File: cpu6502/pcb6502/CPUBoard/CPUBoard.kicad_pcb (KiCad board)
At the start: 2 copper layers, 108.5 x 60.8 mm, 26 parts, among them J1 Expansion, J3 DC Power, J4 Ext Pwr Sw, SW1 Reset, U2 6502 (CPU), U3 28C256 (ROM), U4 L7805, U5 62256 (RAM), U6 DS1813, X1 1MHz

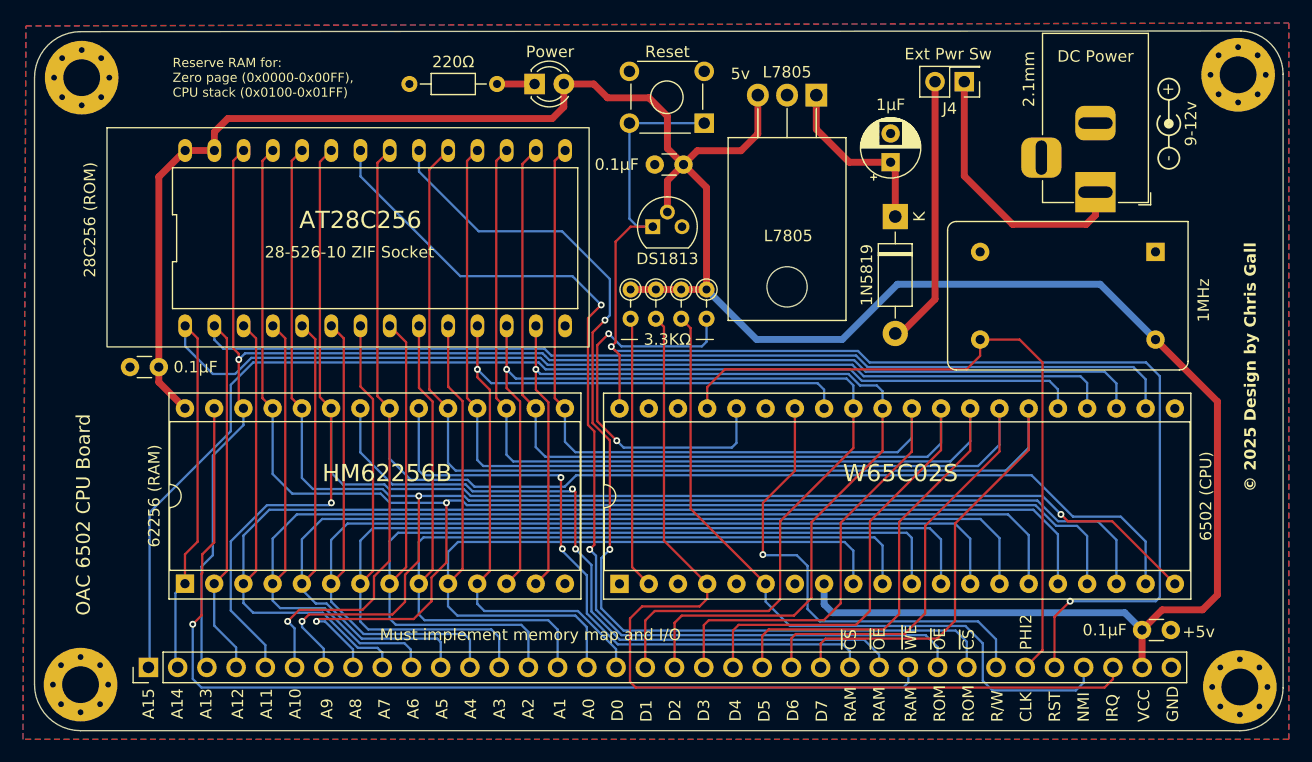
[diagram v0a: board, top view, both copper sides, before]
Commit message: dialed in zeropage and inputbuffer length
PCB CPU BOARD SENT WOOOO HOOO!!
tweaked basic tokens
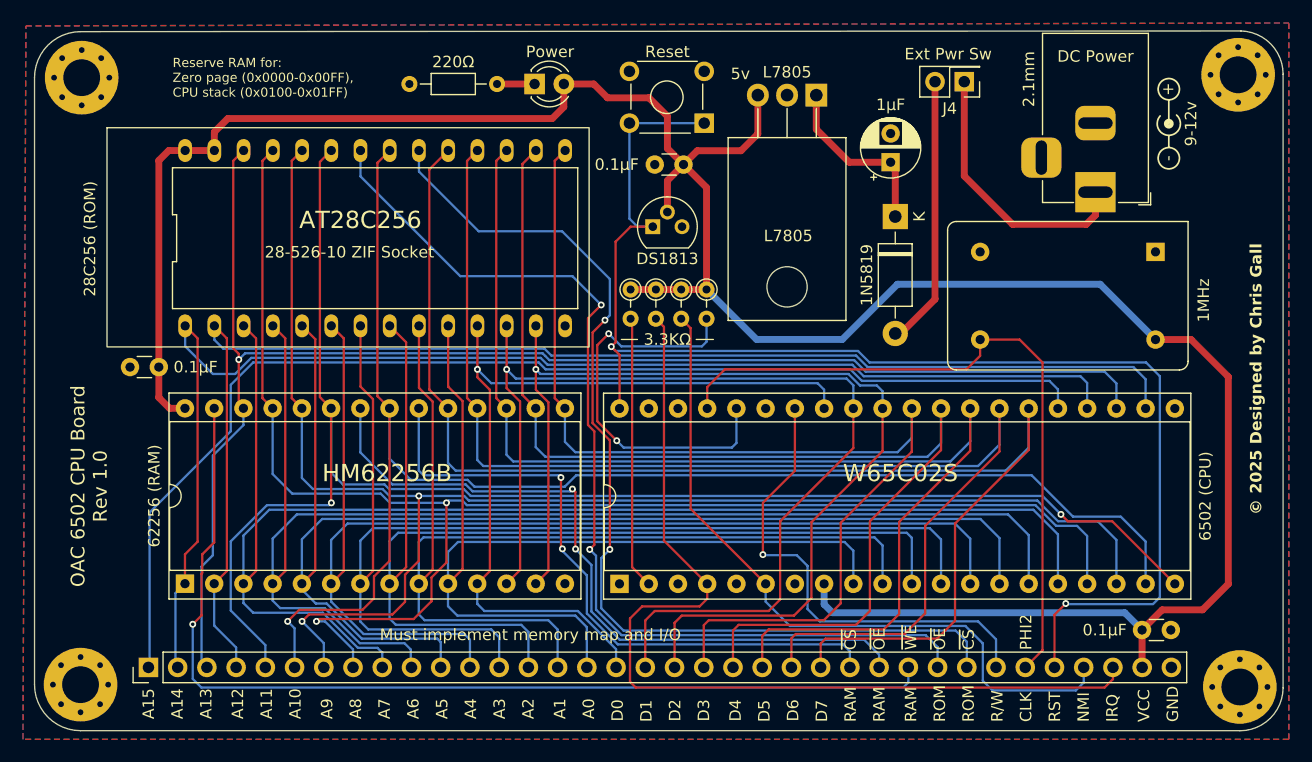
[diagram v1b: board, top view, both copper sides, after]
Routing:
- net +5V: track 221.6 -> 225.8 mm
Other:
- board text added: "OAC 6502 CPU Board Rev 1.0"
- board text added: "© 2025 Designed by Chris Gall"
- board text removed: "+5v"
- board text removed: "OAC 6502 CPU Board"
- board text removed: "Thanks Ben Eater for the Inspiration https://eater.net"
- board text removed: "© 2025 Design by Chris Gall"
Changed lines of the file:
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@@
 		)
 		(property "Value" "6502 (CPU)"
-			(at 7.62 50.96 90)
+			(at 7.62 50.91 90)
 			(layer "F.SilkS")
 			(effects
@@
 		)
 		(property "Value" "28C256 (ROM)"
-			(at -24.2 -1.6 -90)
+			(at -24.2 0.05 -90)
 			(layer "F.SilkS")
 			(effects
@@
 		(tags "C Disc series Radial pin pitch 2.50mm  diameter 3.0mm width 1.6mm Capacitor")
 		(property "Reference" "C3"
-			(at 4.6 0 360)
+			(at 4.6 0 0)
 			(layer "F.Fab")
 			(effects
@@
 		)
 		(property "Value" "0.1µF"
-			(at -3.25 0 360)
+			(at -3.25 0 0)
 			(layer "F.SilkS")
 			(effects
@@
 		)
 		(fp_text user "${REFERENCE}"
-			(at 1.25 0 360)
+			(at 1.25 0 0)
 			(layer "F.Fab")
 			(effects
@@
 		(layer "Edge.Cuts")
 	)
-	(gr_text "Thanks Ben Eater for the Inspiration\nhttps://eater.net"
-		(at 113.75 65.5 90)
-		(layer "B.SilkS")
-		(effects
-			(font
-				(size 0.8 0.8)
-				(thickness 0.1)
-				(bold yes)
-			)
-			(justify left bottom mirror)
-		)
-	)
 	(gr_text "D2 "
 		(at 165.25 98.2 90)
@@
 		)
 	)
-	(gr_text "OAC 6502 CPU Board\n"
-		(at 113.25 89 90)
+	(gr_text "OAC 6502 CPU Board \nRev 1.0\n"
+		(at 113.75 77.75 90)
 		(layer "F.SilkS")
 		(effects
@@
 				(thickness 0.15)
 			)
-			(justify left)
 		)
 	)
@@
 		)
 	)
-	(gr_text "© 2025 Design by Chris Gall"
-		(at 215.25 78.25 90)
+	(gr_text "© 2025 Designed by Chris Gall"
+		(at 215.75 80.25 90)
 		(layer "F.SilkS")
 		(effects
@@
 		)
 	)
-	(gr_text "+5v"
-		(at 208.75 91 0)
-		(layer "F.SilkS")
-		(effects
-			(font
-				(size 1 1)
-				(thickness 0.15)
-			)
-			(justify left bottom)
-		)
-	)
 	(gr_text "IRQ"
 		(at 203.25 98.25 90)
@@
 	)
 	(segment
-		(start 119.8 50.87)
-		(end 119.8 67.4)
-		(width 0.6)
-		(layer "F.Cu")
-		(net 3)
-	)
-	(segment
 		(start 171.86 43.77)
 		(end 171.86 47.14)
@@
 	)
 	(segment
-		(start 119.8 67.4)
-		(end 119.8 68.71)
+		(start 165.4 49.8)
+		(end 164 48.4)
 		(width 0.6)
 		(layer "F.Cu")
@@
 	)
 	(segment
-		(start 165.4 49.8)
-		(end 164 48.4)
+		(start 122.09 48.58)
+		(end 120.67 48.58)
 		(width 0.6)
 		(layer "F.Cu")
@@
 	)
 	(segment
-		(start 211.8 87.2)
-		(end 210.5 88.5)
+		(start 119.8 70.05)
+		(end 120.735 70.985)
 		(width 0.6)
 		(layer "F.Cu")
@@
 	)
 	(segment
-		(start 211.8 70.39)
-		(end 211.8 87.2)
+		(start 205.25 90.25)
+		(end 205.25 93.49)
 		(width 0.6)
 		(layer "F.Cu")
@@
 	)
 	(segment
-		(start 205.25 90.25)
-		(end 205.25 93.49)
+		(start 119.8 67.4)
+		(end 119.8 70.05)
+		(width 0.6)
+		(layer "F.Cu")
+		(net 3)
+	)
+	(segment
+		(start 120.67 48.58)
+		(end 119.8 49.45)
 		(width 0.6)
 		(layer "F.Cu")
@@
 	)
 	(segment
+		(start 206.42 65.01)
+		(end 209.51 65.01)
+		(width 0.6)
+		(layer "F.Cu")
+		(net 3)
+	)
+	(segment
+		(start 207 88.5)
+		(end 205.25 90.25)
+		(width 0.6)
+		(layer "F.Cu")
+		(net 3)
+	)
+	(segment
 		(start 170.4 48.6)
 		(end 166.6 48.6)
@@
 	)
 	(segment
-		(start 122.09 48.58)
-		(end 119.8 50.87)
-		(width 0.6)
-		(layer "F.Cu")
-		(net 3)
-	)
-	(segment
 		(start 155 42.8)
 		(end 155 44.8)
@@
 	)
 	(segment
-		(start 206.42 65.01)
-		(end 211.8 70.39)
+		(start 212.75 68.25)
+		(end 212.75 86.25)
 		(width 0.6)
 		(layer "F.Cu")
@@
 	)
 	(segment
-		(start 207 88.5)
-		(end 205.25 90.25)
+		(start 120.735 70.985)
+		(end 122.075 70.985)
 		(width 0.6)
 		(layer "F.Cu")
@@
 	)
 	(segment
-		(start 210.5 88.5)
-		(end 207 88.5)
+		(start 166.6 48.6)
+		(end 165.4 49.8)
 		(width 0.6)
 		(layer "F.Cu")
@@
 	)
 	(segment
-		(start 166.6 48.6)
-		(end 165.4 49.8)
+		(start 119.8 49.45)
+		(end 119.8 67.4)
 		(width 0.6)
 		(layer "F.Cu")
@@
 	)
 	(segment
-		(start 119.8 68.71)
-		(end 122.075 70.985)
+		(start 212.75 86.25)
+		(end 210.5 88.5)
+		(width 0.6)
+		(layer "F.Cu")
+		(net 3)
+	)
+	(segment
+		(start 210.5 88.5)
+		(end 207 88.5)
+		(width 0.6)
+		(layer "F.Cu")
+		(net 3)
+	)
+	(segment
+		(start 209.51 65.01)
+		(end 212.75 68.25)
 		(width 0.6)
 		(layer "F.Cu")
@@
 	)
 	(segment
-		(start 199 87.75)
-		(end 197.64 89.11)
-		(width 0.2)
-		(layer "F.Cu")
-		(net 8)
-	)
-	(segment
-		(start 197.64 89.11)
+		(start 197.64 88.935)
 		(end 197.64 93.5)
 		(width 0.2)
@@
 		(net 8)
 	)
+	(segment
+		(start 198.625 87.95)
+		(end 197.64 88.935)
+		(width 0.2)
+		(layer "F.Cu")
+		(net 8)
+	)
 	(via
-		(at 199 87.75)
+		(at 198.625 87.95)
 		(size 0.6)
 		(drill 0.3)
@@
 	)
 	(segment
-		(start 206.8 68.2)
-		(end 205.6 67)
+		(start 198.675 88)
+		(end 206.2 88)
 		(width 0.2)
 		(layer "B.Cu")
@@
 	)
 	(segment
-		(start 180.565686 66)
-		(end 159.5 66)
+		(start 206.2 88)
+		(end 206.8 87.4)
 		(width 0.2)
 		(layer "B.Cu")
@@
 	)
 	(segment
-		(start 160.7 46.2)
-		(end 160.7 54.5)
+		(start 181.565686 67)
+		(end 180.565686 66)
 		(width 0.2)
 		(layer "B.Cu")
@@
 	)
 	(segment
-		(start 160.7 54.5)
-		(end 161.4 55.2)
+		(start 206.8 87.4)
+		(end 206.8 68.2)
 		(width 0.2)
 		(layer "B.Cu")
@@
 	)
 	(segment
-		(start 161.4 55.2)
-		(end 162.73 55.2)
+		(start 205.6 67)
+		(end 181.565686 67)
 		(width 0.2)
 		(layer "B.Cu")
@@
 	)
 	(segment
-		(start 205.6 67)
-		(end 181.565686 67)
+		(start 206.8 68.2)
+		(end 205.6 67)
 		(width 0.2)
 		(layer "B.Cu")
@@
 	)
 	(segment
-		(start 159.5 66)
-		(end 159.125 65.625)
+		(start 160.7 46.2)
+		(end 160.7 54.5)
 		(width 0.2)
 		(layer "B.Cu")
@@
 	)
 	(segment
-		(start 181.565686 67)
-		(end 180.565686 66)
+		(start 160.7 54.5)
+		(end 161.4 55.2)
 		(width 0.2)
 		(layer "B.Cu")
@@
 	)
 	(segment
-		(start 199 87.75)
-		(end 206.45 87.75)
+		(start 161.4 55.2)
+		(end 162.73 55.2)
 		(width 0.2)
 		(layer "B.Cu")
@@
 	)
 	(segment
-		(start 206.8 87.4)
-		(end 206.8 68.2)
+		(start 198.625 87.95)
+		(end 198.675 88)
 		(width 0.2)
 		(layer "B.Cu")
@@
 	)
 	(segment
-		(start 206.45 87.75)
-		(end 206.8 87.4)
+		(start 180.565686 66)
+		(end 159.5 66)
+		(width 0.2)
+		(layer "B.Cu")
+		(net 8)
+	)
+	(segment
+		(start 159.5 66)
+		(end 159.125 65.625)
 		(width 0.2)
 		(layer "B.Cu")
@@
 	)
 	(segment
-		(start 132.25 90)
-		(end 134.14 91.89)
+		(start 146.73863 79)
+		(end 146.33863 78.6)
 		(width 0.2)
 		(layer "B.Cu")
@@
 	)
 	(segment
-		(start 146.73863 79)
-		(end 146.33863 78.6)
+		(start 196.151471 79)
+		(end 146.73863 79)
 		(width 0.2)
 		(layer "B.Cu")
@@
 	)
 	(segment
-		(start 196.151471 79)
-		(end 146.73863 79)
+		(start 132.25 89.5)
+		(end 134.14 91.39)
 		(width 0.2)
 		(layer "B.Cu")
@@
 	)
 	(segment
-		(start 132.25 89.5)
-		(end 132.25 90)
+		(start 134.14 91.39)
+		(end 134.14 93.5)
 		(width 0.2)
 		(layer "B.Cu")
@@
 		(width 0.2)
 		(layer "B.Cu")
-		(net 22)
-	)
-	(segment
-		(start 134.14 91.89)
-		(end 134.14 93.5)
-		(width 0.2)
-		(layer "B.Cu")
